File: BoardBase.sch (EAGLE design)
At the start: 5 parts, among them J1 SQT-109

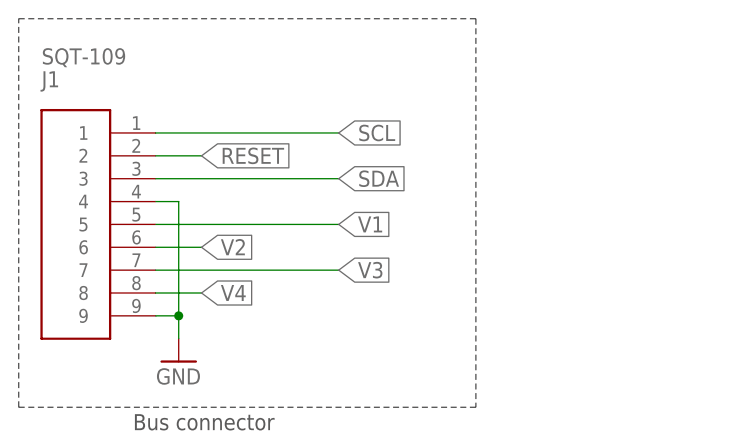
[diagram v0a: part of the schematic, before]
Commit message: Updated PQ9 to support RS-485
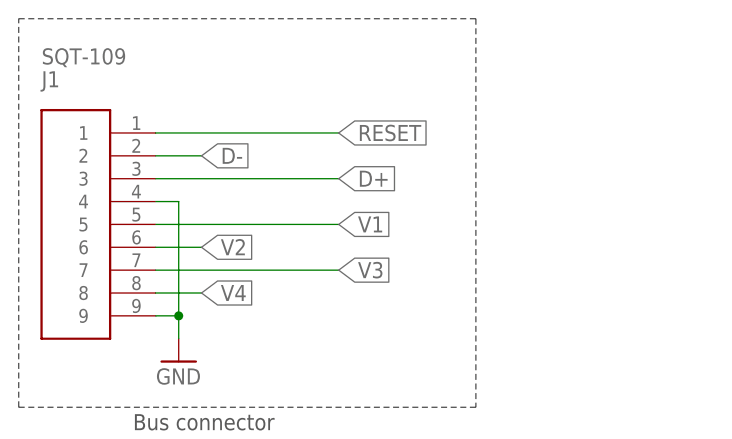
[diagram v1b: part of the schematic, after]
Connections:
- net SDA renamed D+
- removed net SCL: J1.1
- new net D-: J1.2
- net RESET: now also J1.1; no longer J1.2
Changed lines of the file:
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@@
 </busses>
 <nets>
-<net name="SCL" class="0">
+<net name="RESET" class="0">
 <segment>
 <pinref part="J1" gate="G$1" pin="1"/>
@@
 </segment>
 </net>
-<net name="SDA" class="0">
+<net name="D+" class="0">
 <segment>
 <pinref part="J1" gate="G$1" pin="3"/>
@@
 </segment>
 </net>
-<net name="RESET" class="0">
+<net name="D-" class="0">
 <segment>
 <pinref part="J1" gate="G$1" pin="2"/>

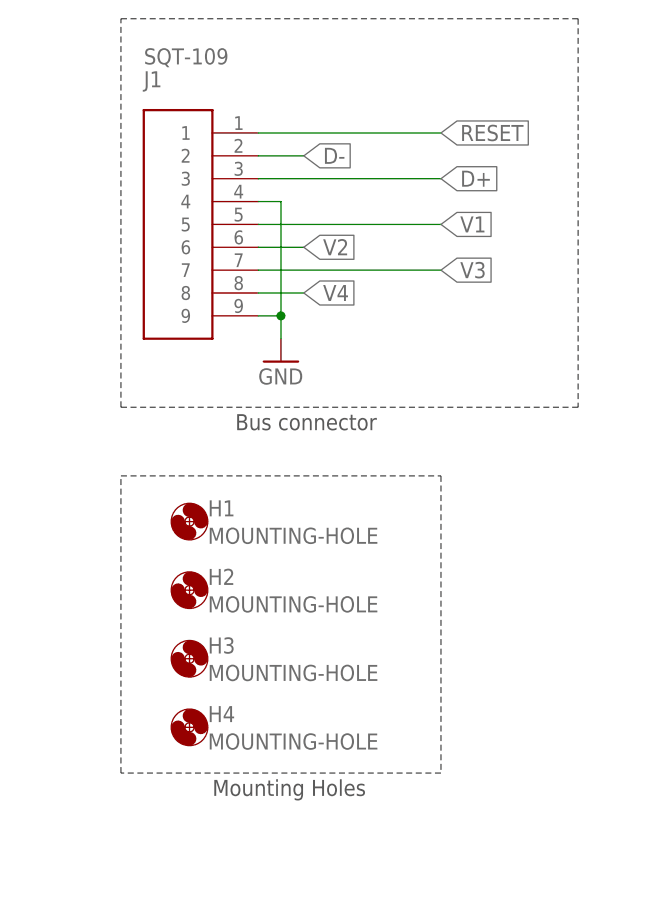
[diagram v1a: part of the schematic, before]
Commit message: Updated template
New components from library
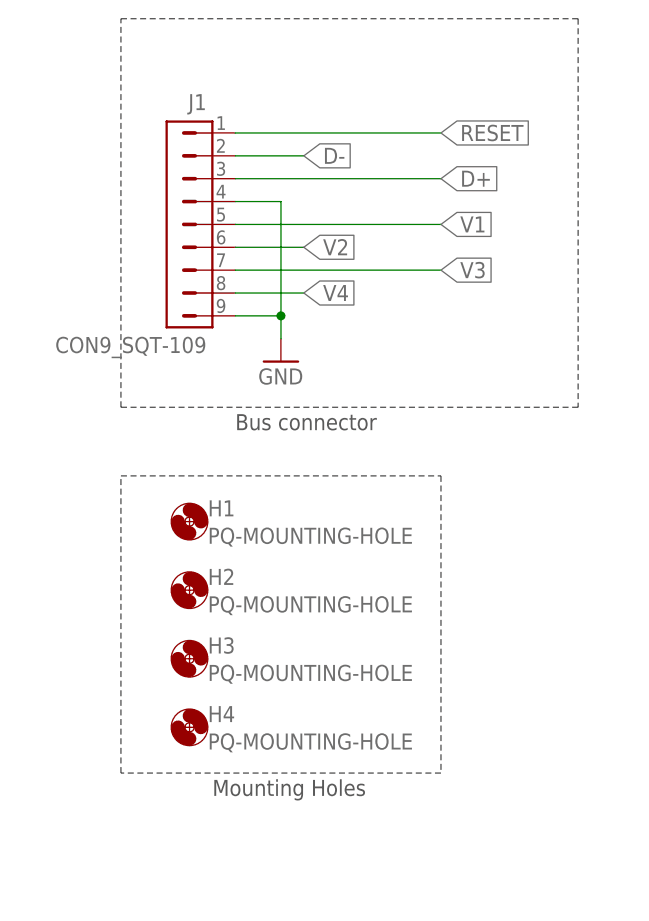
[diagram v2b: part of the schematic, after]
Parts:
- H1, H2, H3, H4: value MOUNTING-HOLE -> PQ-MOUNTING-HOLE; device Delfi-PQ:MOUNTING-HOLE -> Delfi-PQ:PQ-MOUNTING-HOLE
- J1: value SQT-109 -> CON9_SQT-109; device Delfi-PQ:SQT-109 -> Delfi-PQ:CON9_SQT-109

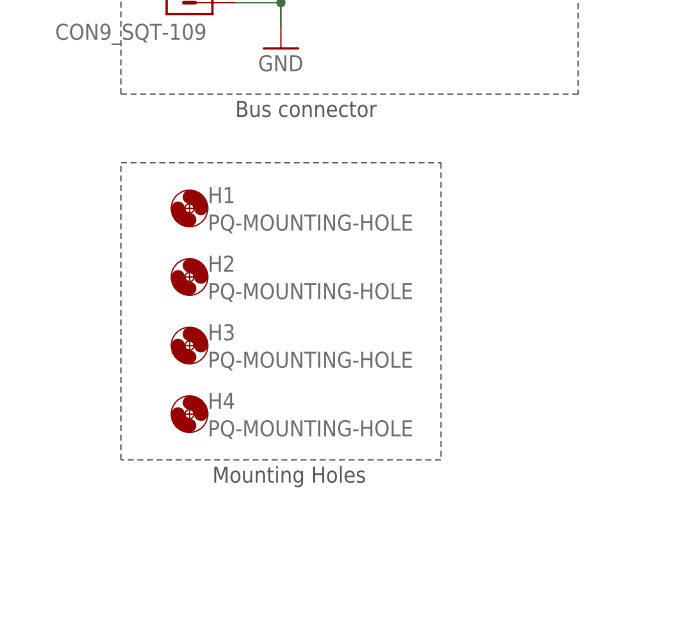
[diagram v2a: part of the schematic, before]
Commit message: Renamed mounting holes
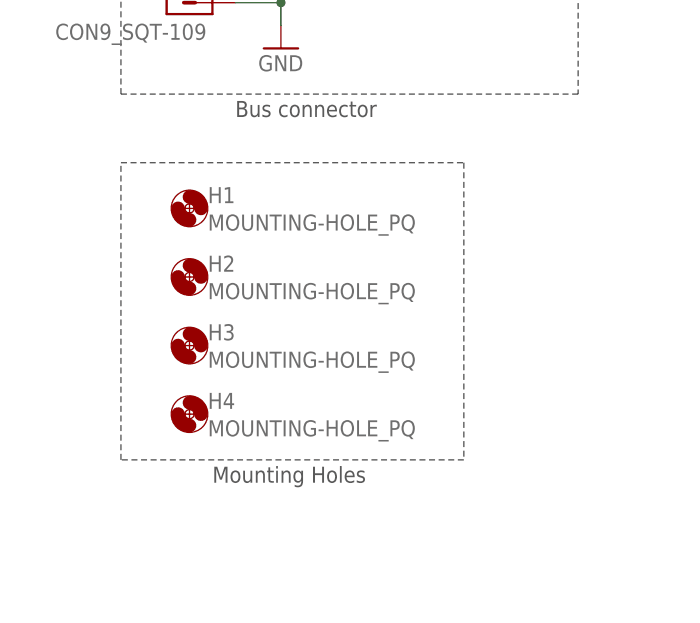
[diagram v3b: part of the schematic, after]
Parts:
- H1, H2, H3, H4: value PQ-MOUNTING-HOLE -> MOUNTING-HOLE_PQ; device Delfi-PQ:PQ-MOUNTING-HOLE -> Delfi-PQ:MOUNTING-HOLE_PQ
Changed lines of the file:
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@@
 <layer number="112" name="tSilk" color="7" fill="1" visible="yes" active="yes"/>
 <layer number="113" name="ReferenceLS" color="7" fill="1" visible="no" active="no"/>
+<layer number="114" name="Al_Dimension" color="7" fill="1" visible="yes" active="yes"/>
+<layer number="115" name="Countersink" color="7" fill="1" visible="yes" active="yes"/>
 <layer number="116" name="Patch_BOT" color="9" fill="4" visible="yes" active="yes"/>
 <layer number="118" name="Rect_Pads" color="7" fill="1" visible="no" active="no"/>
@@
 <part name="J1" library="Delfi-PQ" deviceset="CON9" device="_SQT-109"/>
 <part name="FRAME1" library="frames" deviceset="A4L-LOC" device="" value="TOP frame"/>
-<part name="H1" library="Delfi-PQ" deviceset="PQ-MOUNTING-HOLE" device=""/>
-<part name="H2" library="Delfi-PQ" deviceset="PQ-MOUNTING-HOLE" device=""/>
-<part name="H3" library="Delfi-PQ" deviceset="PQ-MOUNTING-HOLE" device=""/>
-<part name="H4" library="Delfi-PQ" deviceset="PQ-MOUNTING-HOLE" device=""/>
+<part name="H1" library="Delfi-PQ" deviceset="MOUNTING-HOLE" device="_PQ"/>
+<part name="H2" library="Delfi-PQ" deviceset="MOUNTING-HOLE" device="_PQ"/>
+<part name="H3" library="Delfi-PQ" deviceset="MOUNTING-HOLE" device="_PQ"/>
+<part name="H4" library="Delfi-PQ" deviceset="MOUNTING-HOLE" device="_PQ"/>
 <part name="GND1" library="supply1" deviceset="GND" device=""/>
 </parts>
@@
 <sheet>
 <plain>
-<wire x1="-2.54" y1="104.14" x2="33.02" y2="104.14" width="0.1524" layer="97" style="shortdash"/>
-<wire x1="33.02" y1="104.14" x2="33.02" y2="71.12" width="0.1524" layer="97" style="shortdash"/>
-<wire x1="33.02" y1="71.12" x2="-2.54" y2="71.12" width="0.1524" layer="97" style="shortdash"/>
+<wire x1="-2.54" y1="104.14" x2="35.56" y2="104.14" width="0.1524" layer="97" style="shortdash"/>
+<wire x1="35.56" y1="104.14" x2="35.56" y2="71.12" width="0.1524" layer="97" style="shortdash"/>
+<wire x1="35.56" y1="71.12" x2="-2.54" y2="71.12" width="0.1524" layer="97" style="shortdash"/>
 <wire x1="-2.54" y1="71.12" x2="-2.54" y2="104.14" width="0.1524" layer="97" style="shortdash"/>
 <text x="7.62" y="68.58" size="1.778" layer="97">Mounting Holes</text>
